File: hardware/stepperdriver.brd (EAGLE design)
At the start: 100 x 80 mm, 42 parts, among them IC1 L297, IC2 L298, X2 1751248, X3 1751264

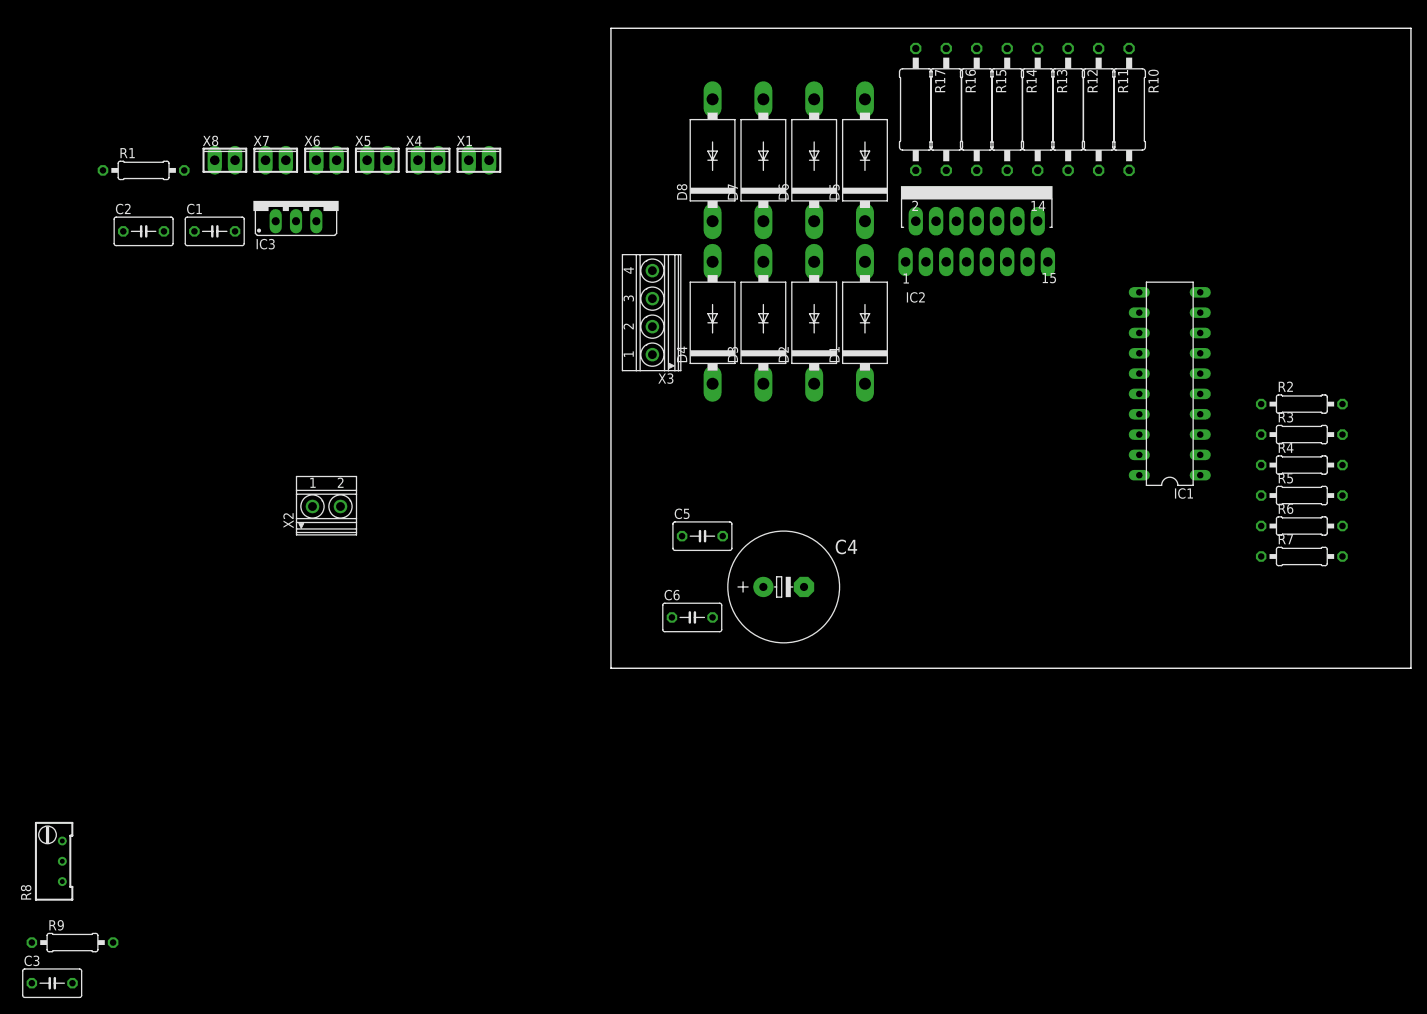
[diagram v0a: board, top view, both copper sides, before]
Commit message: Bauteile grob platziert
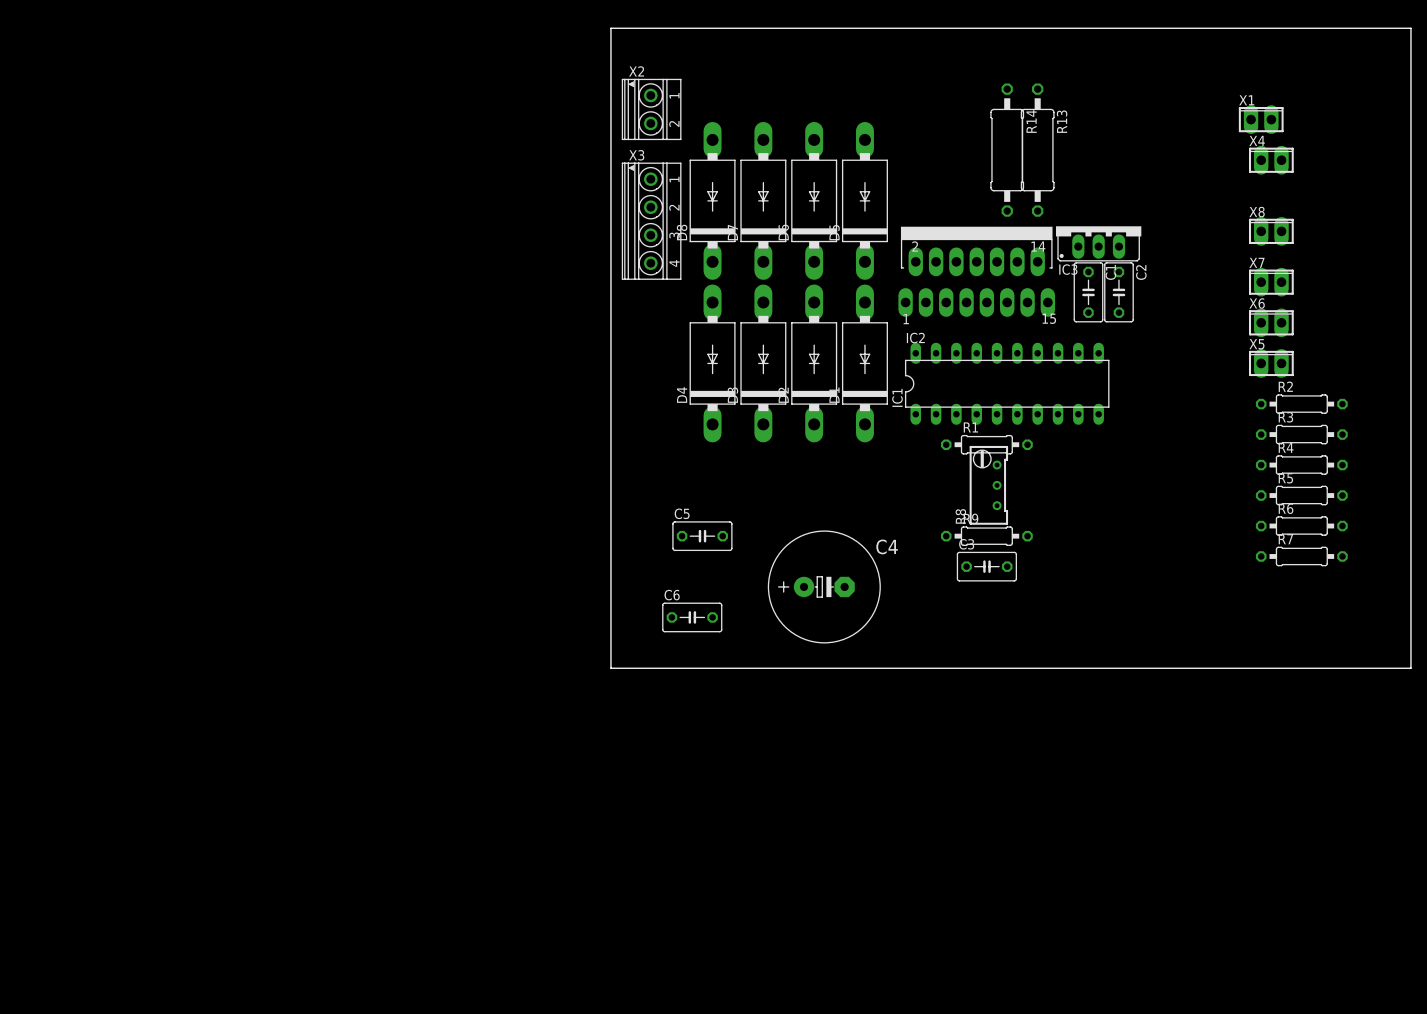
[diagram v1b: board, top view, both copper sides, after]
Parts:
- removed R10, R11, R12, R15, R16, R17: 2.2, resistor:0411/15
- R13, R14: value 2.2 -> 0.51
- moved X8 131.1 mm to (82.5, 54.6)
- moved C3 127.9 mm to (47.0, 12.7)
- moved R8 125.9 mm to (47.0, 22.9)
- moved X7 125.4 mm to (82.5, 48.3)
- moved R9 125.1 mm to (47.0, 16.5)
- moved C2 122.2 mm to (63.5, 47.0), turned to 270 degrees
- moved X6 119.8 mm to (82.5, 43.2)
- moved X5 114.6 mm to (82.5, 38.1)
- moved R1 110.8 mm to (47.0, 27.9)
- moved C1 109.5 mm to (59.7, 47.0), turned to 270 degrees
- moved X4 105.4 mm to (82.5, 63.5)
- moved IC3 100.4 mm to (61.0, 55.2)
- moved X1 97.9 mm to (81.3, 68.6)
- moved X2 64.1 mm to (5.08, 69.8), turned to 270 degrees
- moved IC1 20.3 mm to (49.5, 35.6), turned to 0 degrees
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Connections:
- net GND: no longer R10.1, R11.1, R12.1, R15.1, R16.1, R17.1
- net N$11: no longer R15.2, R16.2, R17.2
- net N$9: no longer R10.2, R11.2, R12.2

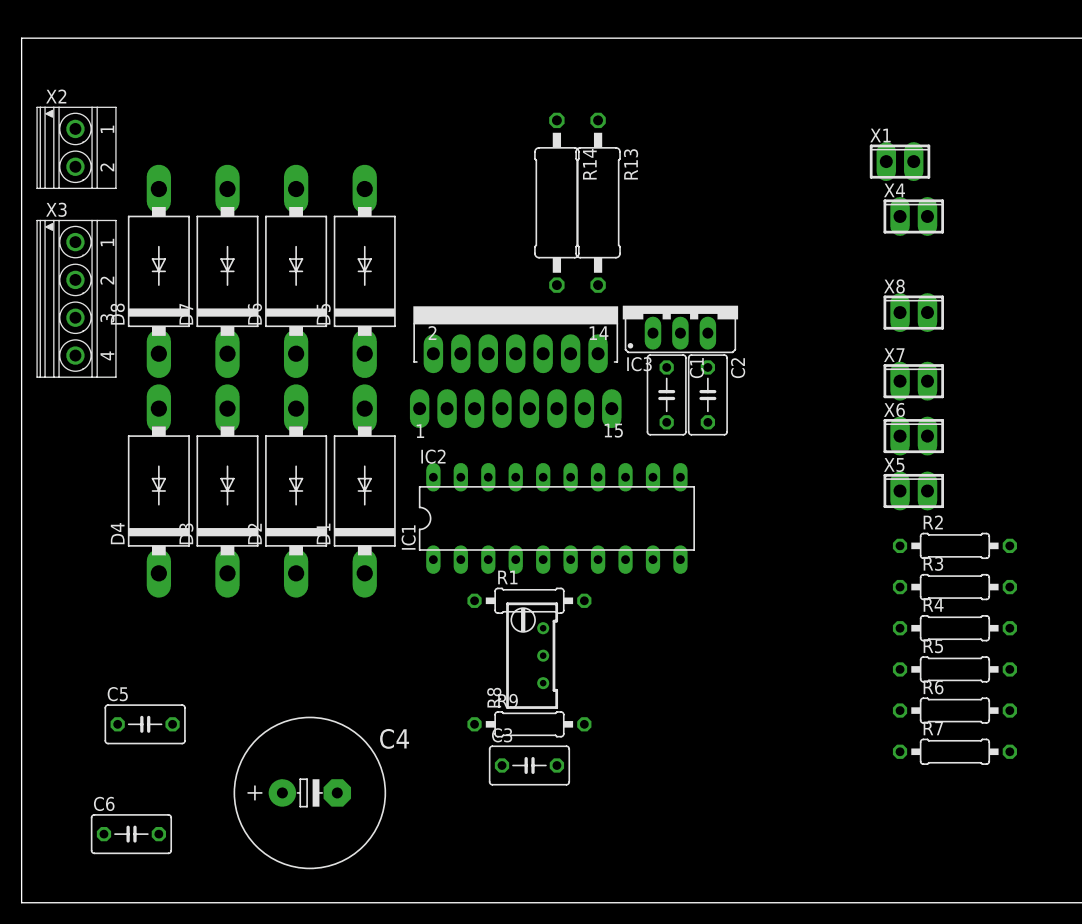
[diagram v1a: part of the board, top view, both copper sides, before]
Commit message: Bauteile platziert
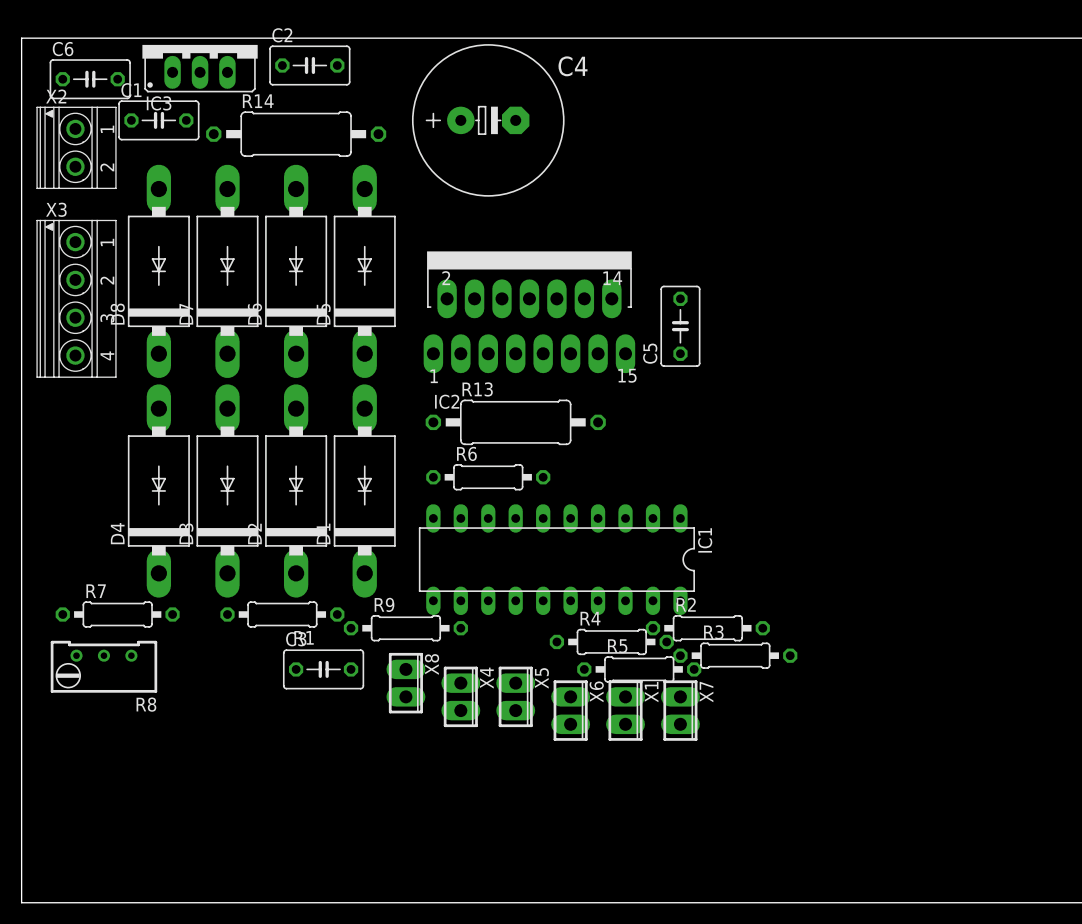
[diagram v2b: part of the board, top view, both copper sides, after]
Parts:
- moved R7 78.5 mm to (8.89, 26.7)
- moved C6 70.0 mm to (6.35, 76.2)
- moved C4 64.4 mm to (43.2, 72.4)
- moved C5 61.7 mm to (61.0, 53.3), turned to 90 degrees
- moved X4 61.1 mm to (40.6, 19.1), turned to 270 degrees
- moved X8 58.2 mm to (35.6, 20.3), turned to 270 degrees
- moved X1 56.8 mm to (55.9, 17.8), turned to 270 degrees
- moved C1 53.4 mm to (12.7, 72.4), turned to 0 degrees
- moved IC3 50.6 mm to (16.5, 79.4)
- moved R6 48.3 mm to (43.2, 39.4)
- moved C2 47.8 mm to (26.7, 77.5), turned to 0 degrees
- moved X5 41.5 mm to (45.7, 19.1), turned to 270 degrees
- moved X6 40.7 mm to (50.8, 17.8), turned to 270 degrees
- moved R8 39.4 mm to (7.62, 21.6), turned to 90 degrees
- moved X7 37.4 mm to (61.0, 17.8), turned to 270 degrees
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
